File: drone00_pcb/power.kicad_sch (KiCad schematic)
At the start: 38 parts, among them J1 USB_B_Micro, J2 BAT, U1 BQ24179YBGR, U3 AMS1117-3.3

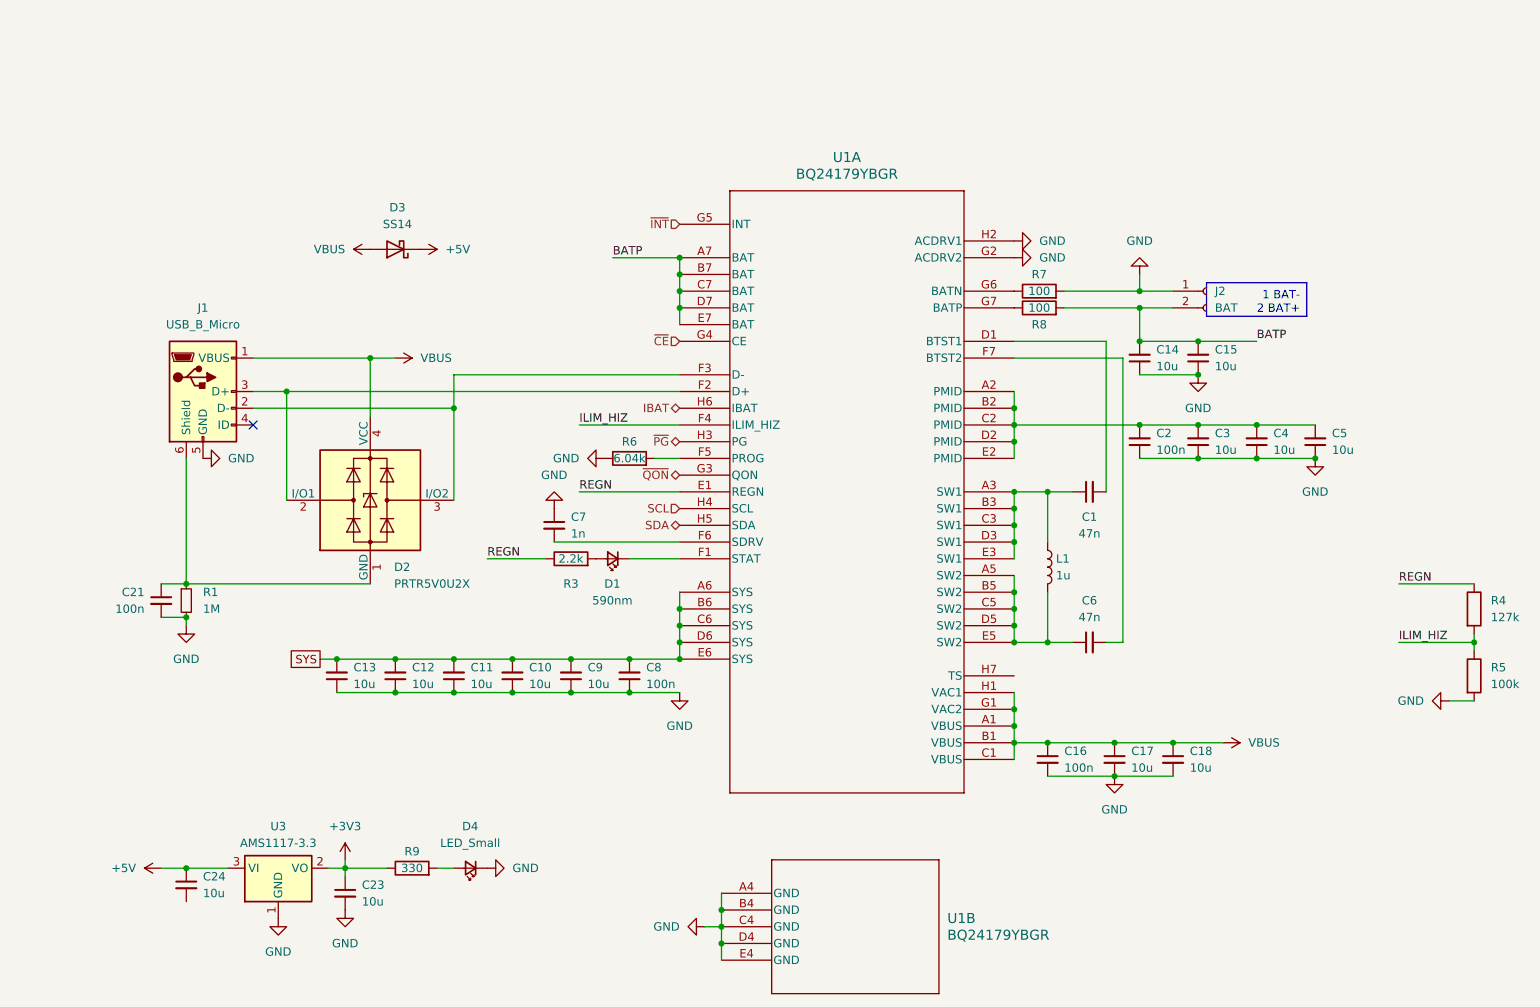
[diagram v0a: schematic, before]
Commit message: Add BQ24
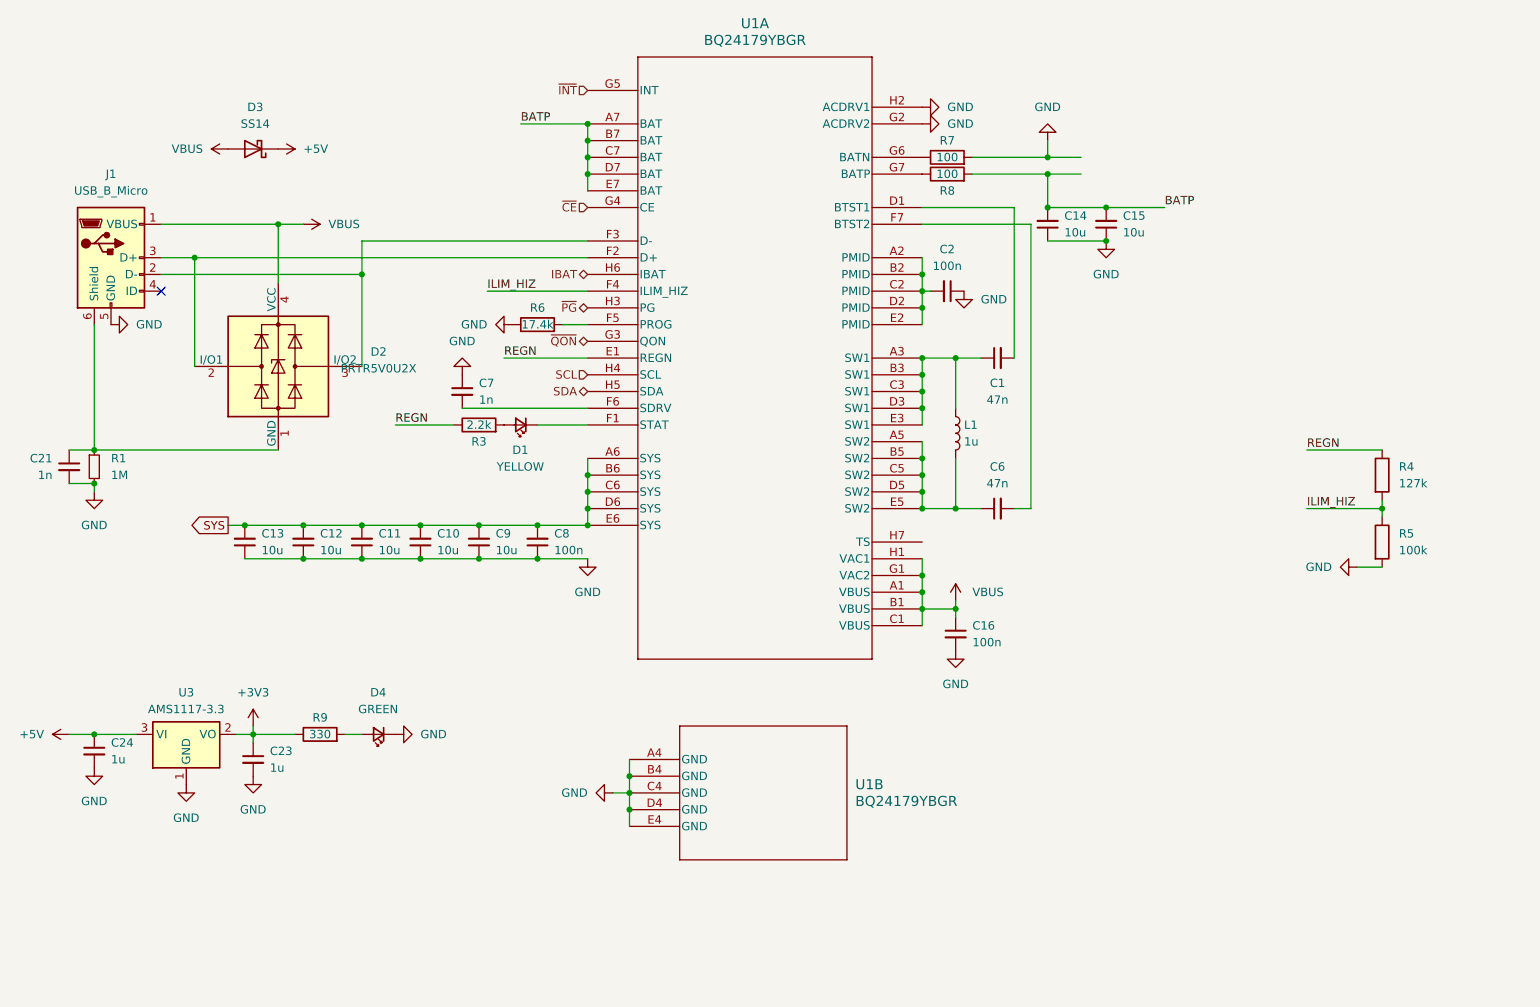
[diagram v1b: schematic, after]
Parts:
- removed C17, C18, C3, C4, C5: 10u, symbol Device:C_Small
- removed J2: BAT, Connector_JST:JST_PH_B2B-PH-K_1x02_P2.00mm_Vertical, symbol Connector:Conn_01x02_Socket
- C1, C6: footprint (none) -> Capacitor_SMD:C_0603_1608Metric; LCSC Part # (none) -> C1622
- C10, C11, C12, C13, C14, C15, C9: footprint (none) -> Capacitor_SMD:C_0603_1608Metric; LCSC Part # (none) -> C96446
- C16, C2, C8: footprint Capacitor_SMD:C_0402_1005Metric -> Capacitor_SMD:C_0603_1608Metric; LCSC Part # (none) -> C14663
- C21: value 100n -> 1n; footprint Capacitor_SMD:C_0402_1005Metric -> Capacitor_SMD:C_1206_3216Metric; LCSC Part # (none) -> C9196
- C23, C24: value 10u -> 1u; footprint (none) -> Capacitor_SMD:C_0402_1005Metric; LCSC Part # (none) -> C52923
- C7: footprint (none) -> Capacitor_SMD:C_0402_1005Metric; LCSC Part # (none) -> C1523
- D1: value 590nm -> YELLOW; footprint (none) -> LED_SMD:LED_0805_2012Metric; LCSC Part # (none) -> C2296
- D2: LCSC Part # (none) -> C2827688
- D3: footprint (none) -> Diode_SMD:D_SMA; LCSC Part # (none) -> C2480
- D4: value LED_Small -> GREEN; footprint (none) -> LED_SMD:LED_0805_2012Metric; LCSC Part # (none) -> C2297
- J1: LCSC Part # (none) -> C132563
- L1: footprint Inductor_SMD:L_0603_1608Metric -> Inductor_SMD:L_0805_2012Metric; LCSC Part # (none) -> C1042
- R1: footprint (none) -> Resistor_SMD:R_0402_1005Metric; LCSC Part # (none) -> C26083
- R3: footprint (none) -> Resistor_SMD:R_0402_1005Metric; LCSC Part # (none) -> C25933
- R5: footprint (none) -> Resistor_SMD:R_0402_1005Metric; LCSC Part # (none) -> C25741
- R6: value 6.04k -> 17.4k
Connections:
- net GND: now also C24.2
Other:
- moved on the sheet: C1, C10, C11, C12, C13, C14, C15, C16, C2, C21, C23, C24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

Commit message: Finish footprints
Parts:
- R4: value 127k -> 100k; footprint (none) -> Resistor_SMD:R_0402_1005Metric; LCSC Part # (none) -> C25741
- R6: footprint (none) -> Resistor_SMD:R_0402_1005Metric; LCSC Part # (none) -> C364849
- R7, R8: footprint (none) -> Resistor_SMD:R_0402_1005Metric; LCSC Part # (none) -> C25076
- R9: footprint (none) -> Resistor_SMD:R_0402_1005Metric; LCSC Part # (none) -> C25104
- U1: LCSC Part # (none) -> C2879484
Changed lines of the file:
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@@
       (effects (font (size 1.27 1.27)))
     )
-    (property "Footprint" "" (at 160.02 39.878 90)
+    (property "Footprint" "Resistor_SMD:R_0402_1005Metric" (at 160.02 39.878 90)
       (effects (font (size 1.27 1.27)) hide)
     )
@@
       (effects (font (size 1.27 1.27)) hide)
     )
-    (property "LCSC Part #" "" (at 160.02 38.1 0)
+    (property "LCSC Part #" "C25076" (at 160.02 38.1 0)
       (effects (font (size 1.27 1.27)) hide)
     )
@@
       (effects (font (size 1.27 1.27)) (justify left))
     )
-    (property "Value" "127k" (at 228.6 85.09 0)
-      (effects (font (size 1.27 1.27)) (justify left))
-    )
-    (property "Footprint" "" (at 224.282 83.82 90)
+    (property "Value" "100k" (at 228.6 85.09 0)
+      (effects (font (size 1.27 1.27)) (justify left))
+    )
+    (property "Footprint" "Resistor_SMD:R_0402_1005Metric" (at 224.282 83.82 90)
       (effects (font (size 1.27 1.27)) hide)
     )
@@
       (effects (font (size 1.27 1.27)) hide)
     )
-    (property "LCSC Part #" "" (at 226.06 83.82 0)
+    (property "LCSC Part #" "C25741" (at 226.06 83.82 0)
       (effects (font (size 1.27 1.27)) hide)
     )
@@
       (effects (font (size 1.27 1.27) italic) hide)
     )
-    (property "LCSC Part #" "" (at 111.76 127 0)
+    (property "LCSC Part #" "C2879484" (at 111.76 127 0)
       (effects (font (size 1.27 1.27)) hide)
     )
@@
       (effects (font (size 1.27 1.27)))
     )
-    (property "Footprint" "" (at 97.79 62.738 90)
+    (property "Footprint" "Resistor_SMD:R_0402_1005Metric" (at 97.79 62.738 90)
       (effects (font (size 1.27 1.27)) hide)
     )
@@
       (effects (font (size 1.27 1.27)) hide)
     )
-    (property "LCSC Part #" "" (at 97.79 60.96 0)
+    (property "LCSC Part #" "C364849" (at 97.79 60.96 0)
       (effects (font (size 1.27 1.27)) hide)
     )
@@
       (effects (font (size 1.27 1.27)))
     )
-    (property "Footprint" "" (at 160.02 37.338 90)
+    (property "Footprint" "Resistor_SMD:R_0402_1005Metric" (at 160.02 37.338 90)
       (effects (font (size 1.27 1.27)) hide)
     )
@@
       (effects (font (size 1.27 1.27)) hide)
     )
-    (property "LCSC Part #" "" (at 160.02 35.56 0)
+    (property "LCSC Part #" "C25076" (at 160.02 35.56 0)
       (effects (font (size 1.27 1.27)) hide)
     )
@@
       (effects (font (size 1.27 1.27) italic) hide)
     )
-    (property "LCSC Part #" "" (at 105.41 25.4 0)
+    (property "LCSC Part #" "C2879484" (at 105.41 25.4 0)
       (effects (font (size 1.27 1.27)) hide)
     )
@@
       (effects (font (size 1.27 1.27)))
     )
-    (property "Footprint" "" (at 64.77 124.968 90)
+    (property "Footprint" "Resistor_SMD:R_0402_1005Metric" (at 64.77 124.968 90)
       (effects (font (size 1.27 1.27)) hide)
     )
@@
       (effects (font (size 1.27 1.27)) hide)
     )
-    (property "LCSC Part #" "" (at 64.77 123.19 0)
-      (effects (font (size 1.27 1.27)) hide)
-    )
+    (property "LCSC Part #" "C25104" (at 64.77 123.19 0)
+      (effects (font (size 1.27 1.27)) hide)
+    )
